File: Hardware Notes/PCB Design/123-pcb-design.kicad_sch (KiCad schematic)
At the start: 2 parts, among them U1 ESP32-C3-MINI-1, U2 MCP73871

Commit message: ADC file added
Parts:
- added 4.7: 4.7μF, symbol Device:C_Small
- added U3: HX711, Package_SO:SOIC-16_3.9x9.9mm_P1.27mm, symbol Analog_ADC:HX711
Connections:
- net at U1.20 (IO6): now also U1.21 (IO7), U2.1 (OUT), U2.20 (OUT), 4.7.1
- new net GND: 4.7.2
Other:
- moved on the sheet: U1, U2

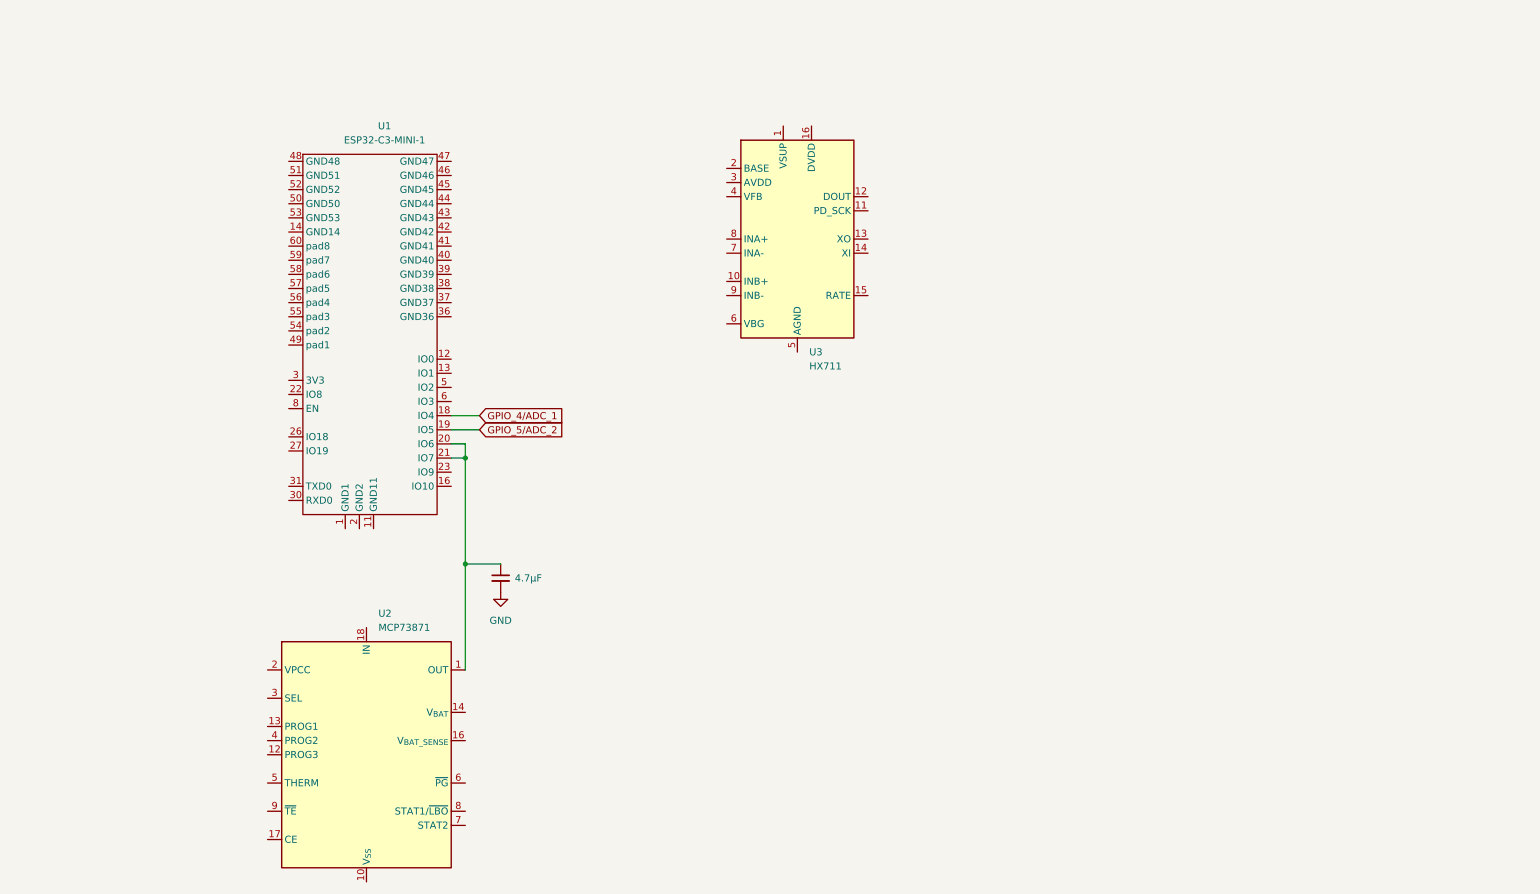
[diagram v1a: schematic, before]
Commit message: USBC connector and HX711 wiring
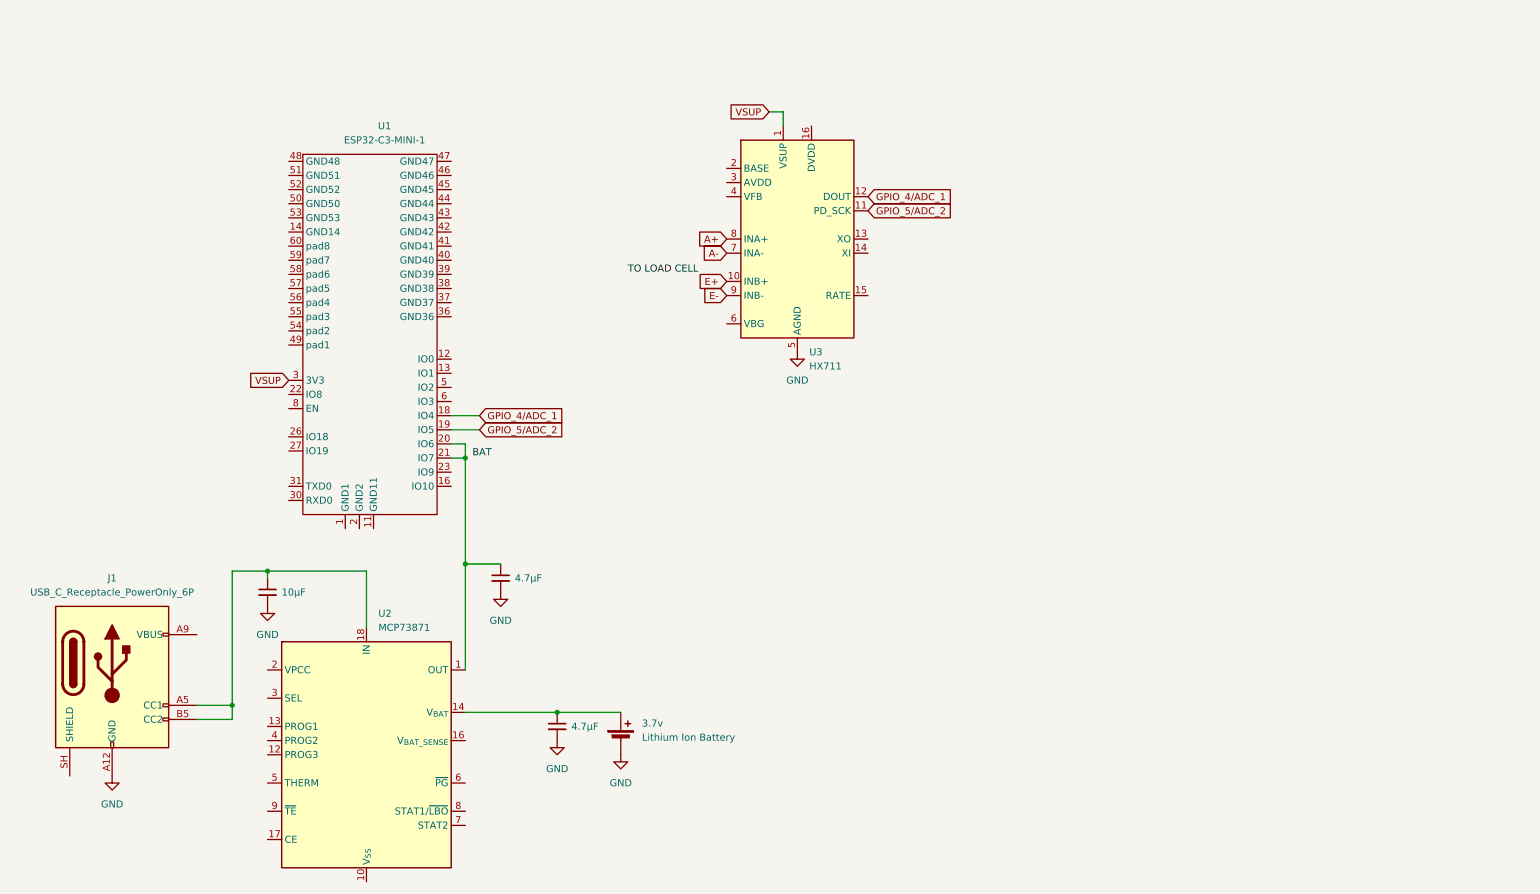
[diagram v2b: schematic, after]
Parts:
- added 3.7v: Lithium Ion Battery, symbol Device:Battery_Cell
- added 4.8: 4.7μF, symbol Device:C_Small
- added 4.9: 10μF, symbol Device:C_Small
- added J1: USB_C_Receptacle_PowerOnly_6P, symbol Connector:USB_C_Receptacle_PowerOnly_6P
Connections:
- net GND: now also U3.5 (AGND), 3.7v.2 (-), 4.8.2, 4.9.2, J1.A12 (GND), J1.B12 (GND)
- net GPIO_4/ADC_1: now also U3.12 (DOUT)
- net GPIO_5/ADC_2: now also U3.11 (PD_SCK)
- net VSUP: now reaches U3.1 (VSUP)
- net VSUP: now also U1.3 (3V3)
- net E+: now reaches U3.10 (INB+)
- net A-: now reaches U3.7 (INA-)
- net A+: now reaches U3.8 (INA+)
- net E-: now reaches U3.9 (INB-)
- net at U2.14 (V_{BAT}), U2.15 (V_{BAT}): now also 3.7v.1 (+), 4.8.1
- net at U2.18 (IN), U2.19 (IN): now also 4.9.1, J1.A5 (CC1), J1.B5 (CC2)
- new net: J1.A9 (VBUS), J1.B9 (VBUS)

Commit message: amplifier circuit added
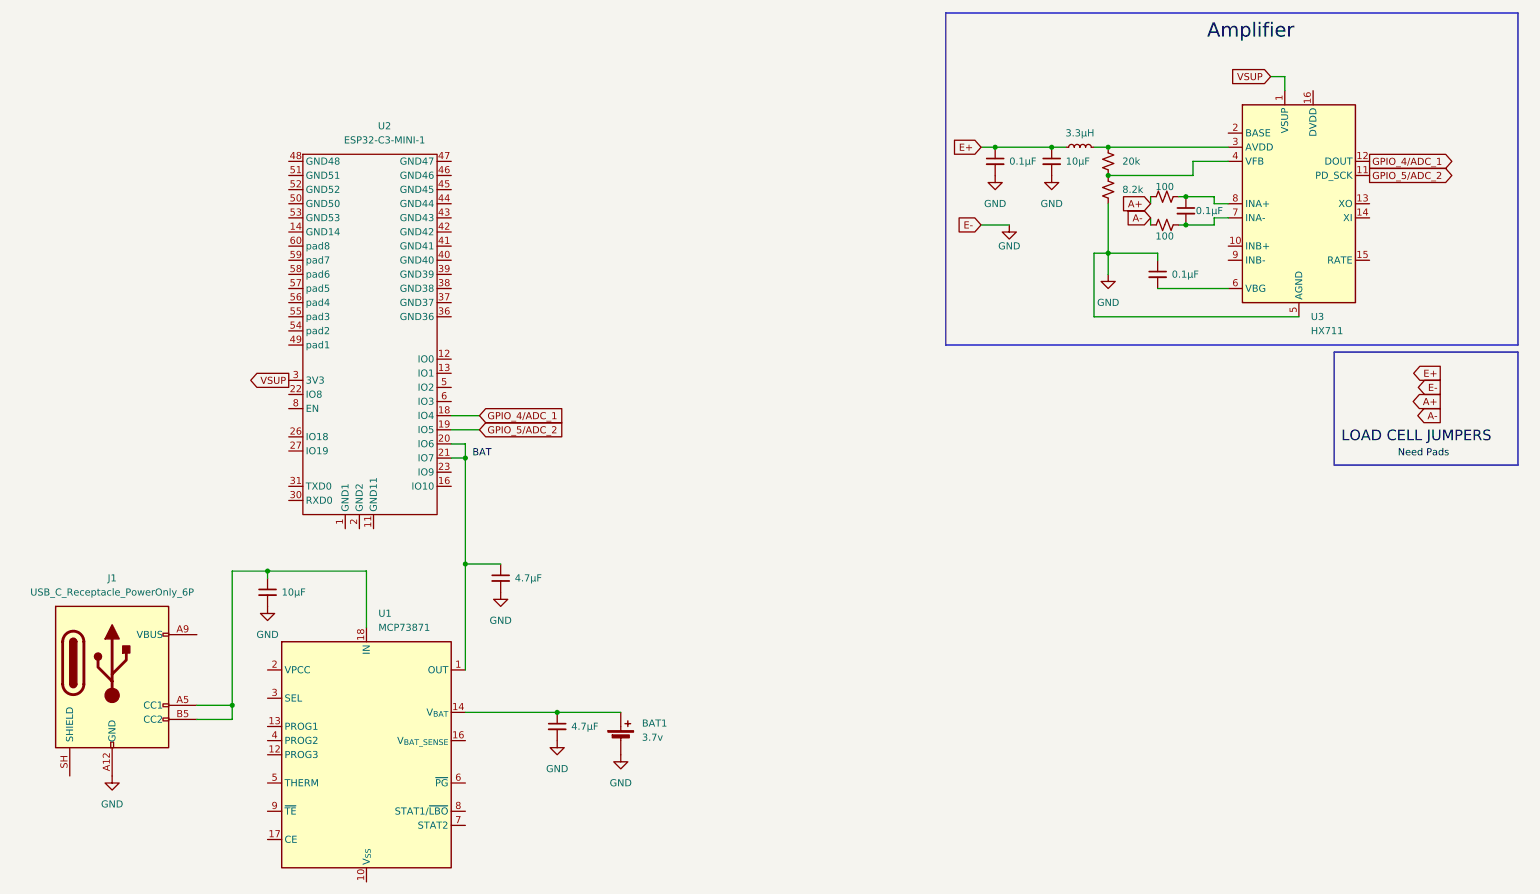
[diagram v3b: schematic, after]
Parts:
- added 4.4, 4.6, 4.7: 0.1μF, symbol Device:C_Small
- added 4.5: 10μF, symbol Device:C_Small
- added L1: 3.3μH, symbol Device:L_Small
- added R1: 20k, symbol Device:R_Small_US
- added R2: 8.2k, symbol Device:R_Small_US
- added R3, R4: 100, symbol Device:R_Small_US
- BAT1: renamed from 3.7v; value Lithium Ion Battery -> 3.7v
- renumbered 4.9 to 4.1, 4.7 to 4.2, 4.8 to 4.3, U2 to U1, U1 to U2
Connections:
- net A+: now also R3.1; no longer U3.8 (INA+)
- net A-: now also R4.1; no longer U3.7 (INA-)
- net E+: now also 4.4.1, 4.5.1, L1.1; no longer U3.10 (INB+)
- net GND: now also 4.4.2, 4.5.2, 4.6.1, R2.2
- net at U3.3 (AVDD): now also L1.2, R1.1
- net at U3.4 (VFB): now also R1.2, R2.1
- net at U3.6 (VBG): now also 4.6.2
- net E-: no longer names the net of U3.9 (INB-)
- new net: 4.7.1, R3.2, U3.8 (INA+)
- new net: 4.7.2, R4.2, U3.7 (INA-)
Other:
- moved on the sheet: U3

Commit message: updated to v1 circuit
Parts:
- removed U2: ESP32-C3-MINI-1, symbol esp32-c3-mini-1:ESP32-C3-MINI-1
- added TP1: E+, symbol Connector:TestPoint
- added TP2: E-, symbol Connector:TestPoint
- added TP3: A+, symbol Connector:TestPoint
- added TP4: A-, symbol Connector:TestPoint
- added U1: ESP32-C3-MINI-1, PCM_Espressif:ESP32-C3-MINI-1, symbol PCM_Espressif:ESP32-C3-MINI-1
- renumbered U1 to U2
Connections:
- net A+: now also TP3.1
- net A-: now also TP4.1
- net E+: now also TP1.1
- net GND: now also TP2.1, U1.1 (GND), U1.11 (GND), U1.14 (GND), U1.2 (GND), U1.36 (GND), U1.37 (GND), U1.38 (GND), U1.39 (GND), U1.40 (GND), U1.41 (GND), U1.42 (GND), U1.43 (GND), U1.44 (GND), U1.45 (GND), U1.46 (GND), U1.47 (GND), U1.48 (GND), U1.49 (GND), U1.50 (GND), U1.51 (GND), U1.52 (GND), U1.53 (GND)
- net GPIO_4/ADC_1: now also U1.18 (GPIO4/ADC1_CH4)
- net GPIO_5/ADC_2: now also U1.19 (GPIO5/ADC2_CH0)
- net VSUP: now also 4.2.1, U2.1 (OUT), U2.20 (OUT), U1.3 (3V3)
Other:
- note added: "Amplifier"
- note added: "LOAD CELL JUMPERS"
- note added: "Shared Power Line"

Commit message: pcb rev2 and routing complete
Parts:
- removed 4.1: 10μF, symbol Device:C_Small
- removed BAT1: 3.7v, symbol Device:Battery_Cell
- removed J1: USB_C_Receptacle_PowerOnly_6P, symbol Connector:USB_C_Receptacle_PowerOnly_6P
- removed TP1: E+, symbol Connector:TestPoint
- removed TP2: E-, symbol Connector:TestPoint
- removed TP3: A+, symbol Connector:TestPoint
- removed TP4: A-, symbol Connector:TestPoint
- added 4.10, 4.11: 10μF, symbol Device:C_Small
- added 4.8, 4.9: 4.7μF, symbol Device:C_Small
- added J1, J2: (no value), symbol Connector:Conn_01x02_Pin
- added J3: Conn_01x04_Pin, symbol Connector:Conn_01x04_Pin
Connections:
- net A+: now also J3.1 (Pin_1)
- net A-: now also J3.2 (Pin_2)
- net E+: now also J3.3 (Pin_3)
- net GND: now also 4.10.2, 4.11.2, 4.8.2, 4.9.2, J3.4 (Pin_4)
- net at U2.18 (IN), U2.19 (IN): now also 4.10.1, 4.11.1, J1.1 (Pin_1), J1.2 (Pin_2)
- net at 4.3.1, U2.14 (V_{BAT}), U2.15 (V_{BAT}): now also U2.16 (V_{BAT_SENSE}), 4.8.1, 4.9.1, J2.1 (Pin_1), J2.2 (Pin_2)
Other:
- note added: "TO BATTERY TERMINALS"
- note added: "TO USB-C POWER"
